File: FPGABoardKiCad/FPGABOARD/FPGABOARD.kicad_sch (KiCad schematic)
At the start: 24 parts, among them J1 USB_C_Receptacle_USB2.0_14P, J2 Conn_02x06_Odd_Even, J3 Conn_02x06_Odd_Even, U1 ICE40HX1K-VQ100, U2 AP2127K-3.3, U3 W25Q32JVSS, U4 AP2127K-1.2, U5 FT2232HPQ, Y2 SG-210STF

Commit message: Schematic Work
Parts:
- added C10, C11, C12, C14, C15, C16, C17, C18, C19, C20, C21, C22, C9: 100n, symbol Device:C_Small
- added C13, C23, C24: 10u, symbol Device:C_Small
- added D1: DONE, symbol Device:LED
- added J4: Program, symbol Connector_Generic:Conn_02x05_Odd_Even
- added R8: 1k, symbol Device:R_Small
- added R9: 10k, symbol Device:R_Small
- added SW1: Reset, symbol Switch:SW_Push
- J2: value Conn_02x06_Odd_Even -> PMOD0
- J3: value Conn_02x06_Odd_Even -> PMOD1
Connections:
- net +1V2: now also U1.11 (VCC), U1.35 (VCC__1), U1.61 (VCC__2), U1.77 (VCC__3), C10.1, C11.1, C12.1, C13.1, C9.1
- net +3V3: now also U1.14 (VCCIO_3__1), U1.22 (VCCIO_3__2), U1.31 (VCCIO_2), U1.38 (VCCIO_2__1), U1.50 (VCC_SPI), U1.58 (VCCIO_1), U1.6 (VCCIO_3), U1.67 (VCCIO_1__1), U1.75 (VPP_2V5), U1.88 (VCCIO_0), U1.92 (VCCIO_0__1), C14.1, C15.1, C16.1, C17.1, C18.1, C19.1, C20.1, C21.1, C22.1, C23.1, C24.1, R8.1, R9.1
- net GND: now also C10.2, C11.2, C12.2, C13.2, C14.2, C15.2, C16.2, C17.2, C18.2, C19.2, C20.2, C21.2, C22.2, C23.2, C24.2, C9.2, D1.1 (K), SW1.2
- net CDONE: now reaches U1.43 (CDONE)
- net CDONE: now also D1.2 (A), R8.2
- net CRESET_B: now reaches U1.44 (CRESET_B)
- net CRESET_B: now also R9.2, SW1.1
- no-connect marks 0 -> 1
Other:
- moved on the sheet: C1, C2, C3, C4, C5, C6, C7, C8, J2, J3, R3, R4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

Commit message: FT2232 Wiring
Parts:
- added C25, C26, C27, C28, C29, C30, C31, C32, C33, C34, C36, C37, C38, C39: 100n, Capacitor_SMD:C_0603_1608Metric, symbol Device:C_Small
- added C35, C40: 10u, Capacitor_SMD:C_0603_1608Metric, symbol Device:C_Small
- added FB1, FB2: 60@100, Inductor_SMD:L_0603_1608Metric, symbol Device:FerriteBead_Small
- added J5: DE15_Pins_HighDensity_MountingHoles, symbol Connector:DE15_Pins_HighDensity_MountingHoles
- added R10: 2k2, Resistor_SMD:R_0603_1608Metric, symbol Device:R_Small
- added R11, R12: 10k, Resistor_SMD:R_0603_1608Metric, symbol Device:R_Small
- added R13: 12k, Resistor_SMD:R_0603_1608Metric, symbol Device:R_Small
- added U6: 93LCxxBxxOT, Package_TO_SOT_SMD:SOT-23-6, symbol Memory_EEPROM:93LCxxBxxOT
- added Y3: SG-210STF, Oscillator:Oscillator_SMD_SeikoEpson_SG210-4Pin_2.5x2.0mm, symbol Oscillator:SG-210STF
- C1, C10, C11, C12, C13, C14, C15, C16, C17, C18, C19, C2, C20, C21, C22, C23, C24, C3, C4, C5, C6, C7, C8, C9: footprint (none) -> Capacitor_SMD:C_0603_1608Metric
- D1: footprint (none) -> LED_SMD:LED_0805_2012Metric
- R1, R2, R3, R4, R5, R6, R7, R8, R9: footprint (none) -> Resistor_SMD:R_0603_1608Metric
- SW1: value Reset -> ResetICE
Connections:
- net +1V2: now also U5.25 (VCORE), U5.44 (VCORE), U5.66 (VCORE), U5.8 (VCORE), C36.1, C38.1, C39.1, C40.1
- net +3V3: now also U5.10 (VCCIO), U5.26 (VCCIO), U5.30 (VREGIN), U5.39 (VCCIO), U5.51 (VCCIO), C25.1, C27.2, C30.1, C31.1, C32.1, C33.1, C34.1, C35.1, FB1.2, FB2.2, R11.1, R12.1, U6.6 (VCC), Y3.1 (~{ST}), Y3.4 (Vcc)
- net CDONE: now also U5.15 (ADBUS6)
- net CRESET_B: now also U5.16 (ADBUS7)
- net D+: now also U5.59 (DP)
- net D-: now also U5.58 (DM)
- net GND: now also U5.29 (GND), U5.3 (TEST), U5.69 (GND), U5.9 (GND), C25.2, C26.2, C27.1, C28.2, C29.2, C30.2, C31.2, C32.2, C33.2, C34.2, C35.2, C36.2, C37.2, C38.2, C39.2, C40.2, R13.1, U6.2 (GND), Y3.2 (GND)
- net ICE_SCK: now also U5.6 (ADBUS0)
- net ICE_SDI: now also U5.11 (ADBUS2)
- net ICE_SDO: now also U5.7 (ADBUS1)
- net ICE_SS: now also U5.13 (ADBUS4)
- net FT_CLK: now reaches U5.1 (EECLK)
- net FT_CLK: now also U6.4 (CLK)
- net FT_DATA: now reaches U5.2 (EEDATA)
- net FT_DATA: now also R10.2, U6.3 (DI)
- net FT_CLOCK: now reaches U5.27 (OSCI)
- net FT_CLOCK: now also C26.1, Y3.3 (OUT)
- net at U5.4 (~{RESET}): now also R12.2
- net SCL: now reaches U5.55 (GPIO1)
- net SDA: now reaches U5.56 (GPIO0)
- net at U5.57 (VCC_USB): now also C28.1, FB1.1
- net at U5.60 (REF): now also R13.2
- net at U5.61 (VCC_PD): now also C29.1, FB2.1
- net FT_CS: now reaches U5.68 (EECS)
- net FT_CS: now also U6.5 (CS)
- new net: R10.1, R11.2, U6.1 (DO)
- no-connect marks 1 -> 39
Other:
- moved on the sheet: C1, C10, C11, C12, C13, C14, C15, C16, C17, C18, C19, C2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

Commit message: Update IO
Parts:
- removed J3: PMOD1, symbol Connector_Generic:Conn_02x06_Odd_Even
- removed J4: Program, symbol Connector_Generic:Conn_02x05_Odd_Even
- removed J5: DE15_Pins_HighDensity_MountingHoles, symbol Connector:DE15_Pins_HighDensity_MountingHoles
- added C41, C42: 100n, Capacitor_SMD:C_0603_1608Metric, symbol Device:C_Small
- added D2: PWRSTATUS, LED_SMD:LED_01005_0402Metric, symbol Device:LED
- added D3: LED0, LED_SMD:LED_01005_0402Metric, symbol Device:LED
- added D4: LED1, LED_SMD:LED_01005_0402Metric, symbol Device:LED
- added D5: LED2, LED_SMD:LED_01005_0402Metric, symbol Device:LED
- added J3: Conn_02x12_Odd_Even, Connector_PinSocket_2.54mm:PinSocket_2x12_P2.54mm_Vertical, symbol Connector_Generic:Conn_02x12_Odd_Even
- added J4: 6PMOD, Connector_PinSocket_2.54mm:PinSocket_1x06_P2.54mm_Horizontal, symbol Connector_Generic:Conn_01x06
- added J5: I2C, Connector_PinSocket_2.54mm:PinSocket_1x04_P2.54mm_Vertical, symbol Connector_Generic:Conn_01x04
- added R14, R15, R16, R17, R19, R20, R21: 10k, Resistor_SMD:R_0603_1608Metric, symbol Device:R_Small
- added R18, R22: 2k2, Resistor_SMD:R_0603_1608Metric, symbol Device:R_Small
- added SW2: BTN0, symbol Switch:SW_Push
- added SW3: BTN1, symbol Switch:SW_Push
- added SW4: BTN2, symbol Switch:SW_Push
- added U7: IS62LV256AL, Package_SO:SOP-28_8.4x18.16mm_P1.27mm, symbol Memory_RAM:IS62C256AL
- D1: footprint LED_SMD:LED_0805_2012Metric -> LED_SMD:LED_01005_0402Metric
- J1: footprint (none) -> Connector_USB:USB_C_Receptacle_G-Switch_GT-USB-7010ASV
- J2: value PMOD0 -> 12PMOD; footprint (none) -> Connector_PinSocket_2.54mm:PinSocket_2x06_P2.54mm_Horizontal
- R9: value 10k -> 5k1
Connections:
- net +3V3: now also J2.1 (Pin_1), J2.2 (Pin_2), C42.1, J3.2 (Pin_2), J3.23 (Pin_23), J4.1 (Pin_1), J5.2 (Pin_2), R14.1, R15.1, R16.1, R17.1, R18.1, R22.1, U7.28 (VDD)
- net +5V: now also J3.1 (Pin_1)
- net CRESET_B: now also C41.1
- net GND: now also J2.3 (Pin_3), J2.4 (Pin_4), C41.2, C42.2, D2.1 (K), D3.1 (K), D4.1 (K), D5.1 (K), J3.24 (Pin_24), J3.4 (Pin_4), J4.2 (Pin_2), J5.1 (Pin_1), SW2.2, SW3.2, SW4.2, U7.14 (GND)
- net SCL: now also J5.3 (Pin_3), R22.2
- net SDA: now also J5.4 (Pin_4), R18.2
- net ICERX: now reaches U5.34 (BDBUS0)
- net ICETX: now reaches U5.35 (BDBUS1)
- net PMOD1: now reaches J2.10 (Pin_10)
- net PMOD4: now reaches J2.11 (Pin_11)
- net PMOD0: now reaches J2.12 (Pin_12)
- net PMOD7: now reaches J2.5 (Pin_5)
- net PMOD3: now reaches J2.6 (Pin_6)
- net PMOD6: now reaches J2.7 (Pin_7)
- net PMOD2: now reaches J2.8 (Pin_8)
- net PMOD5: now reaches J2.9 (Pin_9)
- new net: D5.2 (A), R21.2
- new net: D2.2 (A), R14.2
- new net: D4.2 (A), R20.2
- new net: D3.2 (A), R19.2
- new net BTN0: R15.2, SW2.1
- new net BTN1: R16.2, SW3.1
- new net BTN2: R17.2, SW4.1
- new net EXP0: J3.3 (Pin_3)
- new net EXP1: J3.5 (Pin_5)
- new net EXP10: J3.6 (Pin_6)
- new net EXP11: J3.8 (Pin_8)
- new net EXP12: J3.10 (Pin_10)
- new net EXP13: J3.12 (Pin_12)
- new net EXP14: J3.14 (Pin_14)
- new net EXP15: J3.16 (Pin_16)
- new net EXP16: J3.18 (Pin_18)
- new net EXP17: J3.20 (Pin_20)
- new net EXP18: J3.22 (Pin_22)
- new net EXP2: J3.7 (Pin_7)
- new net EXP3: J3.9 (Pin_9)
- new net EXP4: J3.11 (Pin_11)
- new net EXP5: J3.13 (Pin_13)
- new net EXP6: J3.15 (Pin_15)
- new net EXP7: J3.17 (Pin_17)
- new net EXP8: J3.19 (Pin_19)
- new net EXP9: J3.21 (Pin_21)
- new net LED0: R19.1
- new net LED1: R20.1
- new net LED2: R21.1
- new net PMOD0B: J4.6 (Pin_6)
- new net PMOD1B: J4.5 (Pin_5)
- new net PMOD2B: J4.4 (Pin_4)
- new net PMOD3B: J4.3 (Pin_3)
- new net RAM_CE: U7.20 (~{CE})
- new net RAM_OE: U7.22 (~{OE})
- new net RAM_WE: U7.27 (~{WE})
- no-connect marks 39 -> 37
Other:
- note added: "FT2232Rx <- iCE40Tx"
- note added: "FT2232Tx -> iCE40Rx"
- note added: "Still need to assign based on placement"
- note added: "still need to assign pins"
- moved on the sheet: C1, C10, C11, C12, C13, C14, C15, C16, C17, C18, C19, C2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

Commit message: Some placements
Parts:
- removed C35, C40: 10u, Capacitor_SMD:C_0603_1608Metric, symbol Device:C_Small
- C1, C10, C11, C12, C13, C14, C15, C16, C17, C18, C19, C2, C20, C21, C22, C23, C24, C25, C26, C27, C28, C29, C3, C30, C31, C32, C33, C34, C36, C37, C38, C39, C4, C41, C42, C5, C6, C7, C8, C9: footprint Capacitor_SMD:C_0603_1608Metric -> Capacitor_SMD:C_0805_2012Metric
- D1, D2, D3, D4, D5: footprint LED_SMD:LED_01005_0402Metric -> LED_SMD:LED_1206_3216Metric
- FB1, FB2: footprint Inductor_SMD:L_0603_1608Metric -> Inductor_SMD:L_0805_2012Metric
- R1, R10, R11, R12, R13, R14, R15, R16, R17, R18, R19, R2, R20, R21, R22, R3, R4, R5, R6, R7, R8, R9: footprint Resistor_SMD:R_0603_1608Metric -> Resistor_SMD:R_0805_2012Metric
- SW1, SW2, SW3, SW4: footprint (none) -> Button_Switch_SMD:SW_SPST_PTS647_Sx50
- U2: footprint Package_TO_SOT_SMD:SOT-23-5 -> Package_TO_SOT_SMD:SOT-23-5_HandSoldering
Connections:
- net +1V2: now also C37.1
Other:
- moved on the sheet: J2, J3, J4, J5

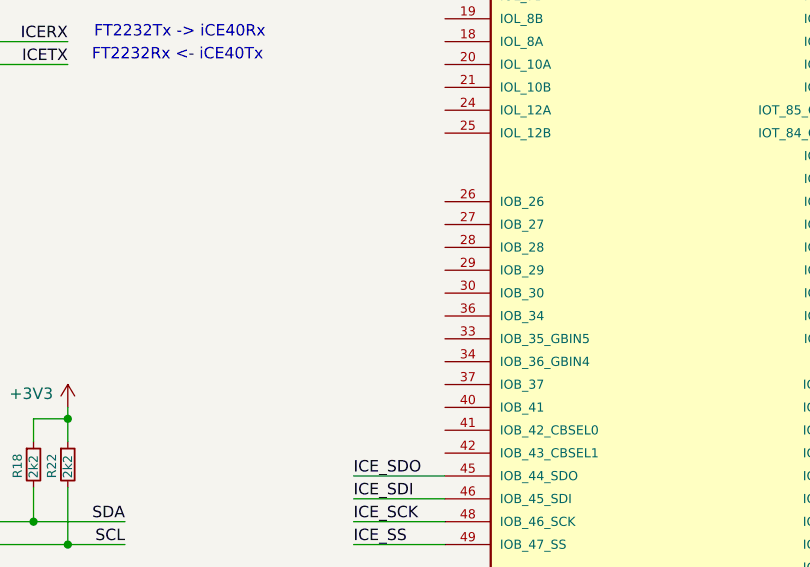
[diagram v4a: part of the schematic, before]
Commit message: Finished placements mostly
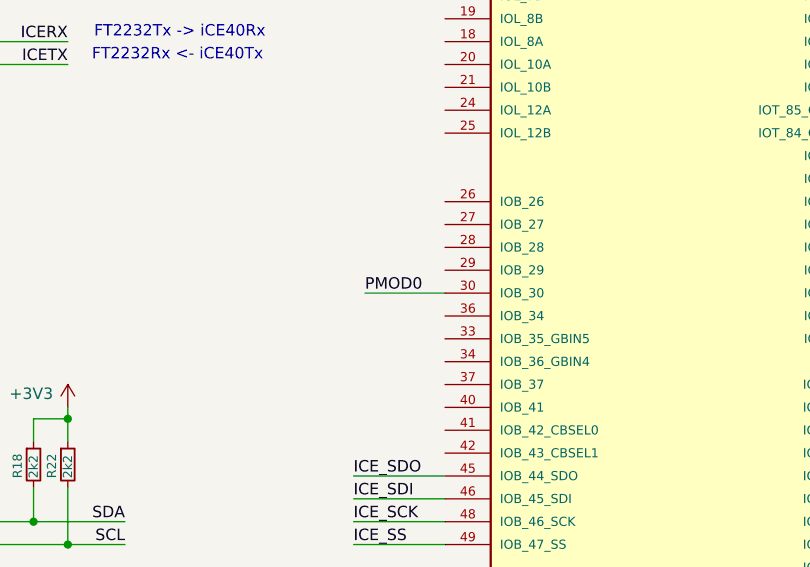
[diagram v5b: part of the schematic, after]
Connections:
- net PMOD0: now also U1.30 (IOB_30)
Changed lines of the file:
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@@
 	(wire
 		(pts
+			(xy 199.39 134.62) (xy 208.28 134.62)
+		)
+		(stroke
+			(width 0)
+			(type default)
+		)
+	)
+	(wire
+		(pts
 			(xy 312.42 57.15) (xy 312.42 54.61)
 		)
@@
 		(effects
 			(font
+				(size 1.27 1.27)
+			)
+			(justify left bottom)
+		)
+	)
+	(label "PMOD0"
+		(at 199.39 134.62 0)
+		(effects
+			(font

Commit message: Finsished up Header and Memory routing
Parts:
- removed C13, C23, C24: 10u, Capacitor_SMD:C_0805_2012Metric, symbol Device:C_Small
- removed C20, C21, C22, C30: 100n, Capacitor_SMD:C_0805_2012Metric, symbol Device:C_Small
- removed J3: Conn_02x12_Odd_Even, Connector_PinSocket_2.54mm:PinSocket_2x12_P2.54mm_Vertical, symbol Connector_Generic:Conn_02x12_Odd_Even
- added J6: Conn_02x13_Odd_Even, Connector_PinSocket_2.54mm:PinSocket_2x13_P2.54mm_Vertical, symbol Connector_Generic:Conn_02x13_Odd_Even
- renumbered C3 to C1, C27 to C10, C28 to C11, C7 to C12, C29 to C13, C36 to C14, C37 to C15, C31 to C16, C38 to C17, C32 to C18, C39 to C19, C1 to C2, C33 to C20, C34 to C21, C42 to C22, C41 to C23, C9 to C24, C14 to C25, C10 to C26, C15 to C27, C11 to C28, C16 to C29, C25 to C3, C17 to C30, C12 to C31, C18 to C32, C19 to C34, C5 to C4, C2 to C5, C4 to C6, C8 to C7, C26 to C8, C6 to C9, FB2 to FB1, FB1 to FB2, J2 to J3, R4 to R1, R11 to R10, R10 to R11, R18 to R12, R22 to R13, R8 to R14, R9 to R15, R14 to R16, R19 to R17, R20 to R18, R21 to R19, R5 to R2, R15 to R20, R16 to R21, R17 to R22, R6 to R4, R7 to R5, R1 to R6, R2 to R7, R13 to R8, R12 to R9, U4 to U1, U6 to U4, U7 to U6, U1 to U7, Y3 to Y1
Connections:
- net +3V3: now also J6.2 (Pin_2), J6.25 (Pin_25)
- net +5V: now also J6.1 (Pin_1)
- net BTN0: now also U7.37 (IOB_37)
- net BTN1: now also U7.40 (IOB_41)
- net BTN2: now also U7.41 (IOB_42_CBSEL0)
- net EXP0: now also U7.12 (IOL_6A), J6.3 (Pin_3)
- net EXP1: now also U7.10 (IOL_5B), J6.5 (Pin_5)
- net EXP10: now also U7.9 (IOL_5A), J6.6 (Pin_6)
- net EXP11: now also U7.7 (IOL_3A), J6.8 (Pin_8)
- net EXP12: now also U7.3 (IOL_2A), J6.10 (Pin_10)
- net EXP13: now also U7.1 (IOL_1A), J6.12 (Pin_12)
- net EXP14: now also U7.99 (IOT_93), J6.14 (Pin_14)
- net EXP15: now also U7.96 (IOT_90), J6.16 (Pin_16)
- net EXP16: now also U7.94 (IOT_88), J6.18 (Pin_18)
- net EXP17: now also U7.93 (IOT_87), J6.20 (Pin_20)
- net EXP18: now also U7.89 (IOT_84_GBIN1), J6.22 (Pin_22)
- net EXP2: now also U7.8 (IOL_3B), J6.7 (Pin_7)
- net EXP3: now also U7.4 (IOL_2B), J6.9 (Pin_9)
- net EXP4: now also U7.2 (IOL_1B), J6.11 (Pin_11)
- net EXP5: now also U7.100 (IOT_95), J6.13 (Pin_13)
- net EXP6: now also U7.97 (IOT_91), J6.15 (Pin_15)
- net EXP7: now also U7.95 (IOT_89), J6.17 (Pin_17)
- net EXP8: now also U7.91 (IOT_86), J6.19 (Pin_19)
- net EXP9: now also U7.87 (IOT_82), J6.21 (Pin_21)
- net GND: now also J6.26 (Pin_26), J6.4 (Pin_4)
- net ICERX: now also U7.15 (IOL_7A_GBIN6)
- net ICETX: now also U7.13 (IOL_6B_GBIN7)
- net LED0: now also U7.36 (IOB_34)
- net LED1: now also U7.34 (IOB_36_GBIN4)
- net LED2: now also U7.33 (IOB_35_GBIN5)
- net PMOD0: now also U7.27 (IOB_27); no longer U7.30 (IOB_30)
- net PMOD0B: now also U7.20 (IOL_10A)
- net PMOD1: now also U7.28 (IOB_28)
- net PMOD1B: now also U7.19 (IOL_8B)
- net PMOD2: now also U7.29 (IOB_29)
- net PMOD2B: now also U7.18 (IOL_8A)
- net PMOD3: now also U7.30 (IOB_30)
- net PMOD3B: now also U7.16 (IOL_7B)
- net PMOD4: now also U7.26 (IOB_26)
- net PMOD5: now also U7.25 (IOL_12B)
- net PMOD6: now also U7.24 (IOL_12A)
- net PMOD7: now also U7.21 (IOL_10B)
- net RAM_CE: now also U7.78 (IOT_73)
- net RAM_OE: now also U7.73 (IOR_71)
- net RAM_WE: now also U7.66 (IOR_65)
- net SCL: now also U7.86 (IOT_81), J6.24 (Pin_24)
- net SDA: now also U7.85 (IOT_80), J6.23 (Pin_23)
- net RAMA14: now reaches U6.1 (A14)
- net RAMA14: now also U7.51 (IOR_52)
- net RAMA0: now reaches U6.10 (A0)
- net RAMA0: now also U7.63 (IOR_61_GBIN2)
- net RAMIO0: now reaches U6.11 (I/O0)
- net RAMIO0: now also U7.64 (IOR_63)
- net RAMIO1: now reaches U6.12 (I/O1)
- net RAMIO1: now also U7.65 (IOR_64)
- net RAMIO2: now reaches U6.13 (I/O2)
- net RAMIO2: now also U7.42 (IOB_43_CBSEL1)
- net RAMIO3: now reaches U6.15 (I/O3)
- net RAMIO3: now also U7.83 (IOT_79)
- net RAMIO4: now reaches U6.16 (I/O4)
- net RAMIO4: now also U7.82 (IOT_78)
- net RAMIO5: now reaches U6.17 (I/O5)
- net RAMIO5: now also U7.81 (IOT_77)
- net RAMIO6: now reaches U6.18 (I/O6)
- net RAMIO6: now also U7.80 (IOT_75)
- net RAMIO7: now reaches U6.19 (I/O7)
- net RAMIO7: now also U7.79 (IOT_74)
- net RAMA12: now reaches U6.2 (A12)
- net RAMA12: now also U7.52 (IOR_53)
- net RAMA10: now reaches U6.21 (A10)
- net RAMA10: now also U7.74 (IOR_72)
- net RAMA11: now reaches U6.23 (A11)
- net RAMA11: now also U7.72 (IOR_70)
- net RAMA9: now reaches U6.24 (A9)
- net RAMA9: now also U7.71 (IOR_69)
- net RAMA8: now reaches U6.25 (A8)
- net RAMA8: now also U7.69 (IOR_68)
- net RAMA13: now reaches U6.26 (A13)
- net RAMA13: now also U7.68 (IOR_67)
- net RAMA7: now reaches U6.3 (A7)
- net RAMA7: now also U7.53 (IOR_54)
- net RAMA6: now reaches U6.4 (A6)
- net RAMA6: now also U7.54 (IOR_55)
- net RAMA5: now reaches U6.5 (A5)
- net RAMA5: now also U7.56 (IOR_56)
- net RAMA4: now reaches U6.6 (A4)
- net RAMA4: now also U7.57 (IOR_57)
- net RAMA3: now reaches U6.7 (A3)
- net RAMA3: now also U7.59 (IOR_58)
- net RAMA2: now reaches U6.8 (A2)
- net RAMA2: now also U7.60 (IOR_59)
- net RAMA1: now reaches U6.9 (A1)
- net RAMA1: now also U7.62 (IOR_60_GBIN3)
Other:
- note removed: "Still need to assign based on placement"
- note removed: "still need to assign pins"
- moved on the sheet: C16, C18, C20, C21

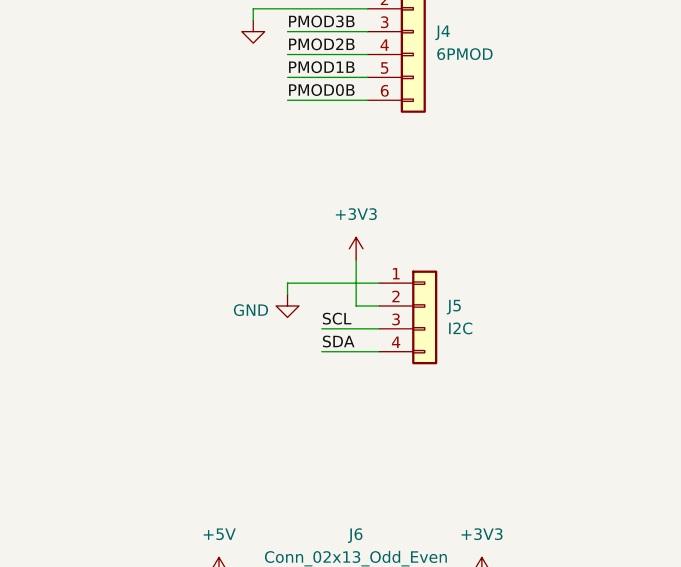
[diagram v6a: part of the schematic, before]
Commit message: Add programing header
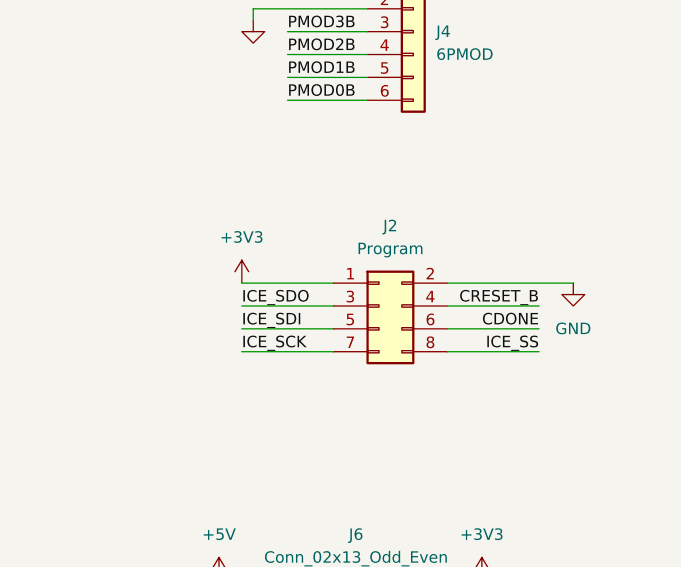
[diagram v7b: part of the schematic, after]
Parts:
- removed J5: I2C, Connector_PinSocket_2.54mm:PinSocket_1x04_P2.54mm_Vertical, symbol Connector_Generic:Conn_01x04
- added J2: Program, Connector_PinSocket_2.54mm:PinSocket_2x04_P2.54mm_Vertical, symbol Connector_Generic:Conn_02x04_Odd_Even
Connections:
- net +3V3: now also J2.1 (Pin_1)
- net CDONE: now also J2.6 (Pin_6)
- net CRESET_B: now also J2.4 (Pin_4)
- net GND: now also J2.2 (Pin_2)
- net ICE_SCK: now also J2.7 (Pin_7)
- net ICE_SDI: now also J2.5 (Pin_5)
- net ICE_SDO: now also J2.3 (Pin_3)
- net ICE_SS: now also J2.8 (Pin_8)
